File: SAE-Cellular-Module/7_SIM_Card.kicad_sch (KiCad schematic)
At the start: 9 parts, among them J4 SIM8066-6-1-14-01-A, U8 EMIF03-SIM02M8

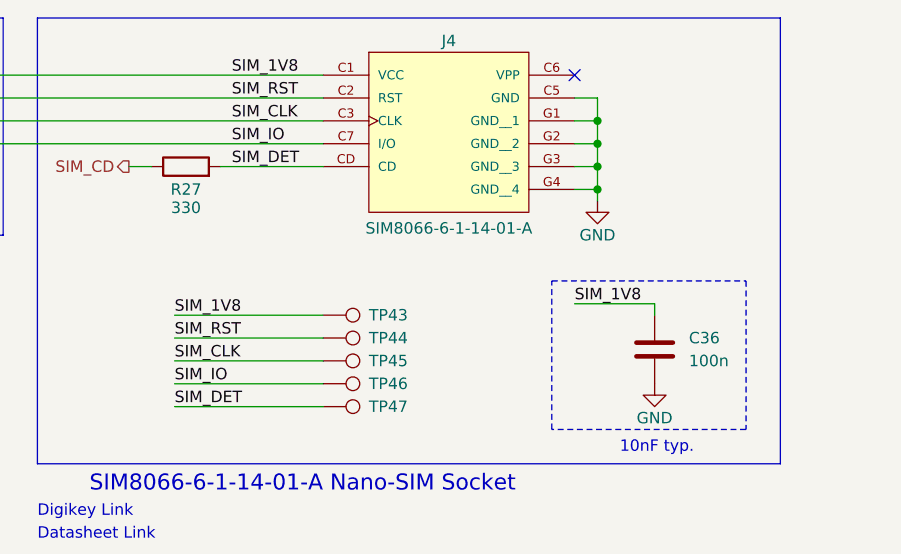
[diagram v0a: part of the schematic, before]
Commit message: Added initial component placements
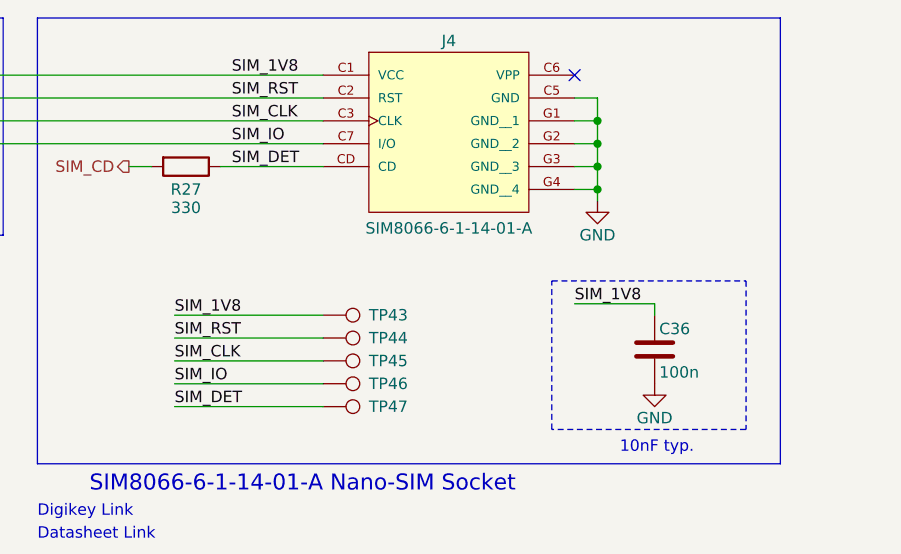
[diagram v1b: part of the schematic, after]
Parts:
- C36: footprint (none) -> Capacitor_SMD:C_0402_1005Metric; MPN (none) -> CL05B104KP5NNNC
- J4: MANUFACTURER Global Connector Technology -> (none); MAXIMUM_PACKAGE_HEIGHT 1.44mm -> (none); MPN (none) -> SIM8066-6-1-14-01-A; PARTREV REVA -> (none); STANDARD Manufacturer recommendations -> (none)
- R27: footprint (none) -> Resistor_SMD:R_0402_1005Metric; MPN (none) -> ERJ-2RKF3300X
- TP43, TP44, TP45, TP46, TP47: footprint (none) -> TestPoint:TestPoint_Pad_D1.0mm
- U8: AVAILABILITY Unavailable -> (none); Check_prices https://www.snapeda.com/parts/EMIF03-SIM02M8/STMicroelectro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 -> (none); DESCRIPTION 3-line EMI filter and ESD protection for SIM card interfaces -> (none); Description_1 RC (Pi) EMI Filter 2nd Order Low Pass 3 Channel R = 47Ohms,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 -> (none); MF STMicroelectronics -> (none); MP EMIF03-SIM02M8 -> (none); MPN (none) -> EMIF03-SIM02M8; PACKAGE UFDFN-8 STMicroelectronics -> (none); PRICE None -> (none); Package UFDFN-8 STMicroelectronics -> (none); SnapEDA_Link https://www.snapeda.com/parts/EMIF03-SIM02M8/STMicroelectro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 -> (none)
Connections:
- net SIM_CD: now also R27.2; no longer R27.1
- net SIM_DET: now also R27.1; no longer R27.2
